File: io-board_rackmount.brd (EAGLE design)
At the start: 480.1 x 90.2 mm, 101 parts

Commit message: changed rackmounted IO board to single 8ch board
to be used with laser-cut mounting panel, or on its own
added pin headers for i2c and channels
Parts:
- removed CH10, CH11, CH12, CH13, CH14, CH15, CH16, CH17, CH18, CH19, CH20, CH21, CH22, CH23, CH24, CH25, CH26, CH27, CH28, CH29, CH30, CH31, CH32, CH9: BNC_VERTICAL, josh:BNC_VERTICAL
- removed LED10, LED11, LED12, LED13, LED14, LED15, LED16, LED17, LED18, LED19, LED20, LED21, LED22, LED23, LED24, LED25, LED26, LED27, LED28, LED29, LED30, LED31, LED32, LED9: (no value), sparkfun:LED3MM
- removed R10, R11, R12, R13, R14, R15, R16, R17, R18, R19, R20, R21, R22, R23, R24, R25, R26, R27, R28, R29, R30, R31, R32, R9: RESISTOR_PTH, josh:RESISTOR_PTH
- removed U$1, U$4, U$5: HDMI, open-ephys:HDMI_A
- added X1: 22-23-2041, con-molex:22-23-2041
- added X3: 22-23-2101, con-molex:22-23-2101
- moved U$2 75.3 mm to (-24.3, 84.3)
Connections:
- removed net CH1: CH10.P$1, R15.P$1, U$1.P$9
- removed net CH2: CH18.P$1, R23.P$1, U$4.P$9
- removed net CH3: CH26.P$1, R31.P$1, U$5.P$9
- removed net N$16: CH14.P$1, R11.P$2, U$1.P$3
- removed net N$17: CH13.P$1, R12.P$2, U$1.P$1
- removed net N$18: CH9.P$1, R16.P$1, U$1.P$7
- removed net N$19: CH11.P$1, R14.P$1, U$1.P$10
- removed net N$20: CH12.P$1, R13.P$1, U$1.P$12
- removed net N$21: CH16.P$1, R9.P$2, U$1.P$6
- removed net N$22: LED9.A, R13.P$2
- removed net N$24: LED10.A, R14.P$2
- removed net N$25: LED11.A, R15.P$2
- removed net N$26: LED12.A, R16.P$2
- removed net N$27: LED13.A, R9.P$1
- removed net N$28: LED14.A, R10.P$1
- removed net N$29: LED15.A, R11.P$1
- removed net N$30: LED16.A, R12.P$1
- removed net N$31: CH23.P$1, R18.P$2, U$4.P$4
- removed net N$32: CH22.P$1, R19.P$2, U$4.P$3
- removed net N$33: CH21.P$1, R20.P$2, U$4.P$1
- removed net N$34: CH17.P$1, R24.P$1, U$4.P$7
- removed net N$35: CH19.P$1, R22.P$1, U$4.P$10
- removed net N$36: CH20.P$1, R21.P$1, U$4.P$12
- removed net N$37: CH24.P$1, R17.P$2, U$4.P$6
- removed net N$38: LED17.A, R21.P$2
- removed net N$39: LED18.A, R22.P$2
- removed net N$40: LED19.A, R23.P$2
- removed net N$41: LED20.A, R24.P$2
- removed net N$42: LED21.A, R17.P$1
- removed net N$43: LED22.A, R18.P$1
- removed net N$44: LED23.A, R19.P$1
- removed net N$45: LED24.A, R20.P$1
- removed net N$46: CH31.P$1, R26.P$2, U$5.P$4
- removed net N$47: CH30.P$1, R27.P$2, U$5.P$3
- removed net N$48: CH29.P$1, R28.P$2, U$5.P$1
- removed net N$49: CH25.P$1, R32.P$1, U$5.P$7
- removed net N$50: CH27.P$1, R30.P$1, U$5.P$10
- removed net N$51: CH28.P$1, R29.P$1, U$5.P$12
- removed net N$52: CH32.P$1, R25.P$2, U$5.P$6
- removed net N$53: LED25.A, R29.P$2
- removed net N$54: LED26.A, R30.P$2
- removed net N$55: LED27.A, R31.P$2
- removed net N$56: LED28.A, R32.P$2
- removed net N$57: LED29.A, R25.P$1
- removed net N$58: LED30.A, R26.P$1
- removed net N$59: LED31.A, R27.P$1
- removed net N$6: CH15.P$1, R10.P$2, U$1.P$4
- removed net N$60: LED32.A, R28.P$1
- new net I2C_CLK: U$3.P$15, X1.3
- new net I2C_DAT: U$3.P$16, X1.4
- new net VCC: U$3.P$18, X1.2
- net CH6: now also X3.7
- net DGND: now also X1.1, X3.1, X3.10; no longer CH10.P$2, CH11.P$2, CH12.P$2, CH13.P$2, CH14.P$2, CH15.P$2, CH16.P$2, CH17.P$2, CH18.P$2, CH19.P$2, CH20.P$2, CH21.P$2, CH22.P$2, CH23.P$2, CH24.P$2, CH25.P$2, CH26.P$2, CH27.P$2, CH28.P$2, CH29.P$2, CH30.P$2, CH31.P$2, CH32.P$2, CH9.P$2, LED10.K, LED11.K, LED12.K, LED13.K, LED14.K, LED15.K, LED16.K, LED17.K, LED18.K, LED19.K, LED20.K, LED21.K, LED22.K, LED23.K, LED24.K, LED25.K, LED26.K, LED27.K, LED28.K, LED29.K, LED30.K, LED31.K, LED32.K, LED9.K, U$1.P$11, U$1.P$17, U$1.P$2, U$1.P$5, U$1.P$8, U$4.P$11, U$4.P$17, U$4.P$2, U$4.P$5, U$4.P$8, U$5.P$11, U$5.P$17, U$5.P$2, U$5.P$5, U$5.P$8
- net N$2: now also X3.4
- net N$23: now also X3.5
- net N$3: now also X3.3
- net N$4: now also X3.2
- net N$5: now also X3.6
- net N$7: now also X3.8
- net N$8: now also X3.9
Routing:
- net DGND: track 249.0 -> 72.4 mm, vias 14 -> 6
- net N$33: track 102.0 -> 0.00 mm, vias 2 -> 0
- net N$17: track 102.0 -> 0.00 mm, vias 2 -> 0
- net N$48: track 102.0 -> 0.00 mm, vias 2 -> 0
- net DGND2: track 100.6 -> 0.00 mm, vias 3 -> 0
- net N$16: track 100.0 -> 0.00 mm, vias 1 -> 0
- net N$32: track 100.0 -> 0.00 mm, vias 1 -> 0
- net N$47: track 100.0 -> 0.00 mm, vias 1 -> 0
- net N$52: track 82.3 -> 0.00 mm
- net N$37: track 82.3 -> 0.00 mm
- net N$21: track 82.3 -> 0.00 mm
- net N$18: track 81.3 -> 0.00 mm
- net N$49: track 81.3 -> 0.00 mm
- net N$34: track 81.3 -> 0.00 mm
- net S$14: track 0.00 -> 78.9 mm
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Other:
- board size 480.1 x 90.2 mm -> 122.7 x 90.3 mm
- board text added: "1 2 3 4 5 6 7 8"
- board text added: "5vdc"
- board text added: "gnd"
- board text added: "i2c clk"
- board text added: "i2c dat"

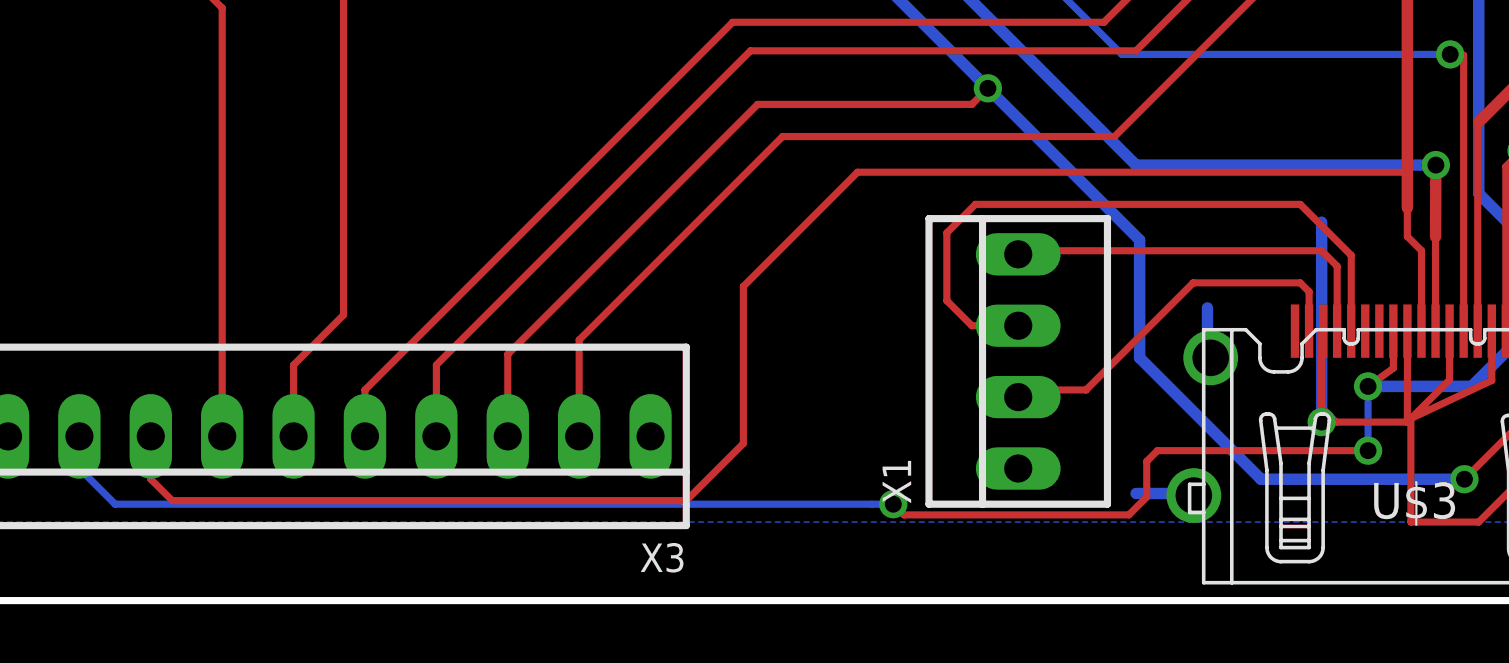
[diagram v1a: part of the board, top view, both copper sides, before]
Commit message: updated .1 inch connector to be linear
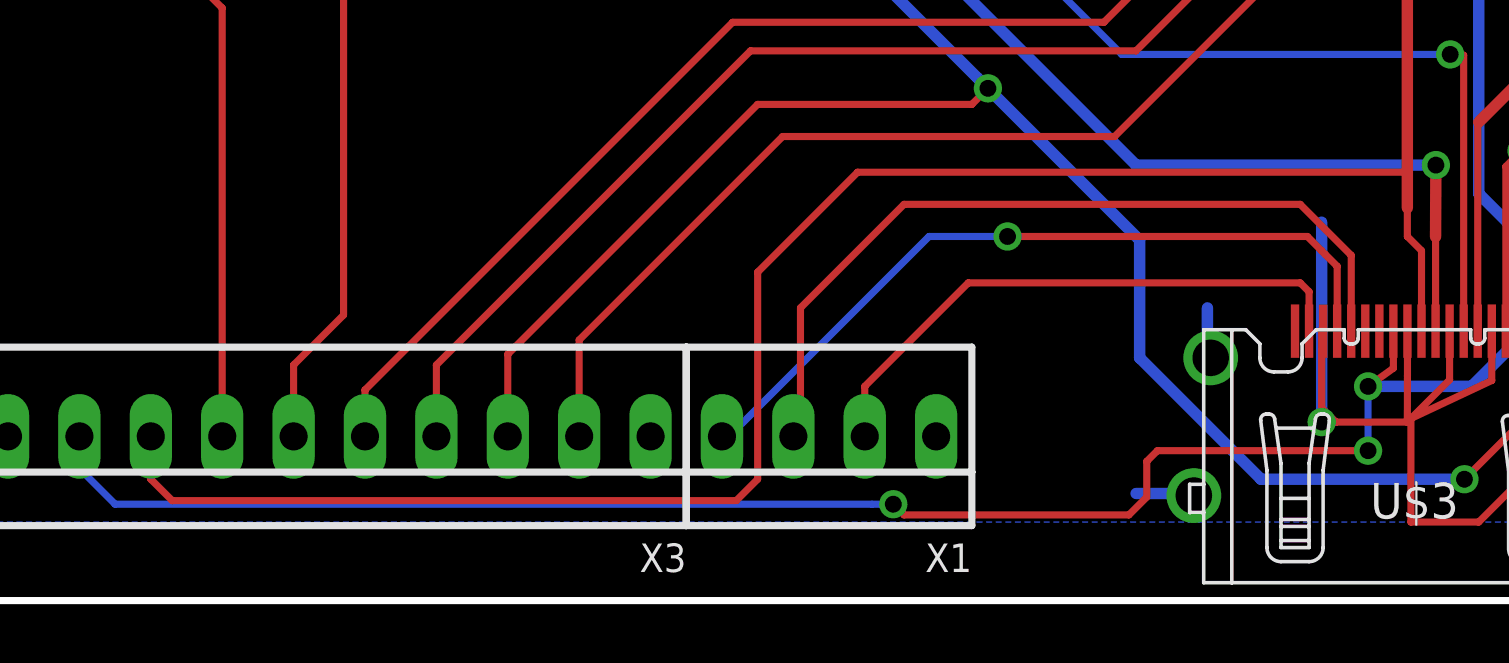
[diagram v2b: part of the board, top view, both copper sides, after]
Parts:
- moved X1 7.24 mm to (7.37, 4.57), turned to 180 degrees
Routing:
- net I2C_DAT: track 13.9 -> 27.6 mm, vias 0 -> 1
- net VCC: track 13.6 -> 20.9 mm
- net I2C_CLK: track 23.6 -> 29.2 mm
- net N$7: track 95.2 -> 96.3 mm
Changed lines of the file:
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@@
 <setting verticaltext="up"/>
 </settings>
-<grid distance="0.01" unitdist="inch" unit="inch" style="lines" multiple="10" display="yes" altdistance="0.025" altunitdist="inch" altunit="inch"/>
+<grid distance="10" unitdist="mil" unit="mil" style="lines" multiple="1" display="yes" altdistance="0.025" altunitdist="inch" altunit="inch"/>
 <layers>
 <layer number="1" name="Top" color="4" fill="1" visible="yes" active="yes"/>
@@
 <layer number="14" name="Route14" color="1" fill="6" visible="no" active="no"/>
 <layer number="15" name="Route15" color="4" fill="6" visible="no" active="no"/>
-<layer number="16" name="Bottom" color="9" fill="1" visible="no" active="yes"/>
+<layer number="16" name="Bottom" color="9" fill="1" visible="yes" active="yes"/>
 <layer number="17" name="Pads" color="2" fill="1" visible="yes" active="yes"/>
 <layer number="18" name="Vias" color="2" fill="1" visible="yes" active="yes"/>
@@
 <text x="68.072" y="45.72" size="6.096" layer="51" font="vector" ratio="16">8</text>
 <rectangle x1="39.624" y1="2.032" x2="73.152" y2="22.352" layer="51"/>
-<text x="6.858" y="2.794" size="1.27" layer="51" font="vector" ratio="12">gnd</text>
-<text x="5.842" y="5.207" size="1.27" layer="51" font="vector" ratio="12">5vdc</text>
-<text x="3.429" y="7.747" size="1.27" layer="51" font="vector" ratio="12">i2c clk</text>
-<text x="3.429" y="10.16" size="1.27" layer="51" font="vector" ratio="12">i2c dat</text>
+<text x="11.43" y="8.89" size="1.27" layer="51" font="vector" ratio="12" rot="R90">gnd</text>
+<text x="9.271" y="8.89" size="1.27" layer="51" font="vector" ratio="12" rot="R90">5vdc</text>
+<text x="6.731" y="8.509" size="1.27" layer="51" font="vector" ratio="12" rot="R90">i2c clk</text>
+<text x="4.318" y="8.255" size="1.27" layer="51" font="vector" ratio="12" rot="R90">i2c dat</text>
 <text x="-19.939" y="42.672" size="1.27" layer="25" font="vector" ratio="12">gnd</text>
 <text x="-21.209" y="8.255" size="1.27" layer="51" font="vector" ratio="12" rot="R90">gnd</text>
@@
 <element name="U$2" library="josh" package="OPEN_EPHYS_LOGO" value="" x="-24.257" y="84.328"/>
 <element name="U$3" library="open-ephys" package="HDMI_A" value="HDMI" x="28.194" y="7.366"/>
-<element name="X1" library="con-molex" package="22-23-2041" value="22-23-2041" x="14.097" y="7.239" rot="R90">
-<attribute name="OC_NEWARK" value="38C0355" x="14.097" y="7.239" size="1.778" layer="27" rot="R90" display="off"/>
-<attribute name="MPN" value="22-23-2041" x="14.097" y="7.239" size="1.778" layer="27" rot="R90" display="off"/>
-<attribute name="MF" value="MOLEX" x="14.097" y="7.239" size="1.778" layer="27" rot="R90" display="off"/>
-<attribute name="OC_FARNELL" value="1462920" x="14.097" y="7.239" size="1.778" layer="27" rot="R90" display="off"/>
+<element name="X1" library="con-molex" package="22-23-2041" value="22-23-2041" x="7.366" y="4.572" rot="R180">
+<attribute name="OC_NEWARK" value="38C0355" x="7.366" y="4.572" size="1.778" layer="27" rot="R180" display="off"/>
+<attribute name="MPN" value="22-23-2041" x="7.366" y="4.572" size="1.778" layer="27" rot="R180" display="off"/>
+<attribute name="MF" value="MOLEX" x="7.366" y="4.572" size="1.778" layer="27" rot="R180" display="off"/>
+<attribute name="OC_FARNELL" value="1462920" x="7.366" y="4.572" size="1.778" layer="27" rot="R180" display="off"/>
 </element>
 <element name="X3" library="con-molex" package="22-23-2101" value="22-23-2101" x="-10.414" y="4.572" rot="R180">
@@
 <wire x1="-16.764" y1="4.572" x2="-16.764" y2="3.048" width="0.254" layer="1"/>
 <wire x1="-16.764" y1="3.048" x2="-16.002" y2="2.286" width="0.254" layer="1"/>
-<wire x1="-16.002" y1="2.286" x2="2.286" y2="2.286" width="0.254" layer="1"/>
-<wire x1="2.286" y1="2.286" x2="4.318" y2="4.318" width="0.254" layer="1"/>
-<wire x1="4.318" y1="4.318" x2="4.318" y2="9.906" width="0.254" layer="1"/>
-<wire x1="4.318" y1="9.906" x2="8.382" y2="13.97" width="0.254" layer="1"/>
+<wire x1="-16.002" y1="2.286" x2="4.064" y2="2.286" width="0.254" layer="1"/>
+<wire x1="4.064" y1="2.286" x2="4.826" y2="3.048" width="0.254" layer="1"/>
+<wire x1="4.826" y1="3.048" x2="4.826" y2="10.414" width="0.254" layer="1"/>
+<wire x1="4.826" y1="10.414" x2="8.382" y2="13.97" width="0.254" layer="1"/>
 <wire x1="8.382" y1="13.97" x2="27.813" y2="13.97" width="0.254" layer="1"/>
 <wire x1="27.813" y1="13.97" x2="27.94" y2="14.097" width="0.254" layer="1"/>
@@
 <wire x1="24.444" y1="8.316" x2="24.444" y2="9.719" width="0.254" layer="1"/>
 <wire x1="24.444" y1="9.719" x2="24.13" y2="10.033" width="0.254" layer="1"/>
-<wire x1="24.13" y1="10.033" x2="20.32" y2="10.033" width="0.254" layer="1"/>
-<wire x1="20.32" y1="10.033" x2="16.51" y2="6.223" width="0.254" layer="1"/>
-<wire x1="16.51" y1="6.223" x2="14.351" y2="6.223" width="0.254" layer="1"/>
-<wire x1="14.351" y1="6.223" x2="14.097" y2="5.969" width="0.254" layer="1"/>
+<wire x1="24.13" y1="10.033" x2="12.319" y2="10.033" width="0.254" layer="1"/>
+<wire x1="12.319" y1="10.033" x2="8.636" y2="6.35" width="0.254" layer="1"/>
+<wire x1="8.636" y1="6.35" x2="8.636" y2="4.318" width="0.254" layer="1"/>
+<wire x1="8.636" y1="4.318" x2="8.636" y2="4.572" width="0" layer="19" extent="1-1"/>
 </signal>
 <signal name="I2C_CLK">
@@
 <wire x1="25.944" y1="8.316" x2="25.944" y2="11.013" width="0.254" layer="1"/>
 <wire x1="25.944" y1="11.013" x2="24.13" y2="12.827" width="0.254" layer="1"/>
-<wire x1="24.13" y1="12.827" x2="12.573" y2="12.827" width="0.254" layer="1"/>
-<wire x1="12.573" y1="12.827" x2="11.557" y2="11.811" width="0.254" layer="1"/>
-<wire x1="11.557" y1="11.811" x2="11.557" y2="9.398" width="0.254" layer="1"/>
-<wire x1="11.557" y1="9.398" x2="12.446" y2="8.509" width="0.254" layer="1"/>
-<wire x1="12.446" y1="8.509" x2="14.097" y2="8.509" width="0.254" layer="1"/>
+<wire x1="24.13" y1="12.827" x2="10.033" y2="12.827" width="0.254" layer="1"/>
+<wire x1="10.033" y1="12.827" x2="6.35" y2="9.144" width="0.254" layer="1"/>
+<wire x1="6.35" y1="9.144" x2="6.35" y2="4.826" width="0.254" layer="1"/>
+<wire x1="6.35" y1="4.826" x2="6.096" y2="4.572" width="0.254" layer="1"/>
 </signal>
 <signal name="I2C_DAT">
@@
 <contactref element="U$3" pad="P$16"/>
 <wire x1="25.444" y1="8.316" x2="25.444" y2="10.624" width="0.254" layer="1"/>
-<wire x1="25.444" y1="10.624" x2="24.892" y2="11.176" width="0.254" layer="1"/>
-<wire x1="24.892" y1="11.176" x2="14.224" y2="11.176" width="0.254" layer="1"/>
-<wire x1="14.224" y1="11.176" x2="14.097" y2="11.049" width="0.254" layer="1"/>
+<wire x1="25.444" y1="10.624" x2="25.019" y2="11.049" width="0.254" layer="1"/>
+<wire x1="25.019" y1="11.049" x2="24.892" y2="11.176" width="0.254" layer="1"/>
+<wire x1="3.556" y1="4.572" x2="3.81" y2="4.572" width="0.254" layer="16"/>
+<wire x1="3.81" y1="4.572" x2="10.922" y2="11.684" width="0.254" layer="16"/>
+<wire x1="10.922" y1="11.684" x2="13.716" y2="11.684" width="0.254" layer="16"/>
+<via x="13.716" y="11.684" extent="1-16" drill="0.6" shape="square"/>
+<wire x1="13.716" y1="11.684" x2="24.384" y2="11.684" width="0.254" layer="1"/>
+<wire x1="24.384" y1="11.684" x2="24.892" y2="11.176" width="0.254" layer="1"/>
 </signal>
 <signal name="DGND1">

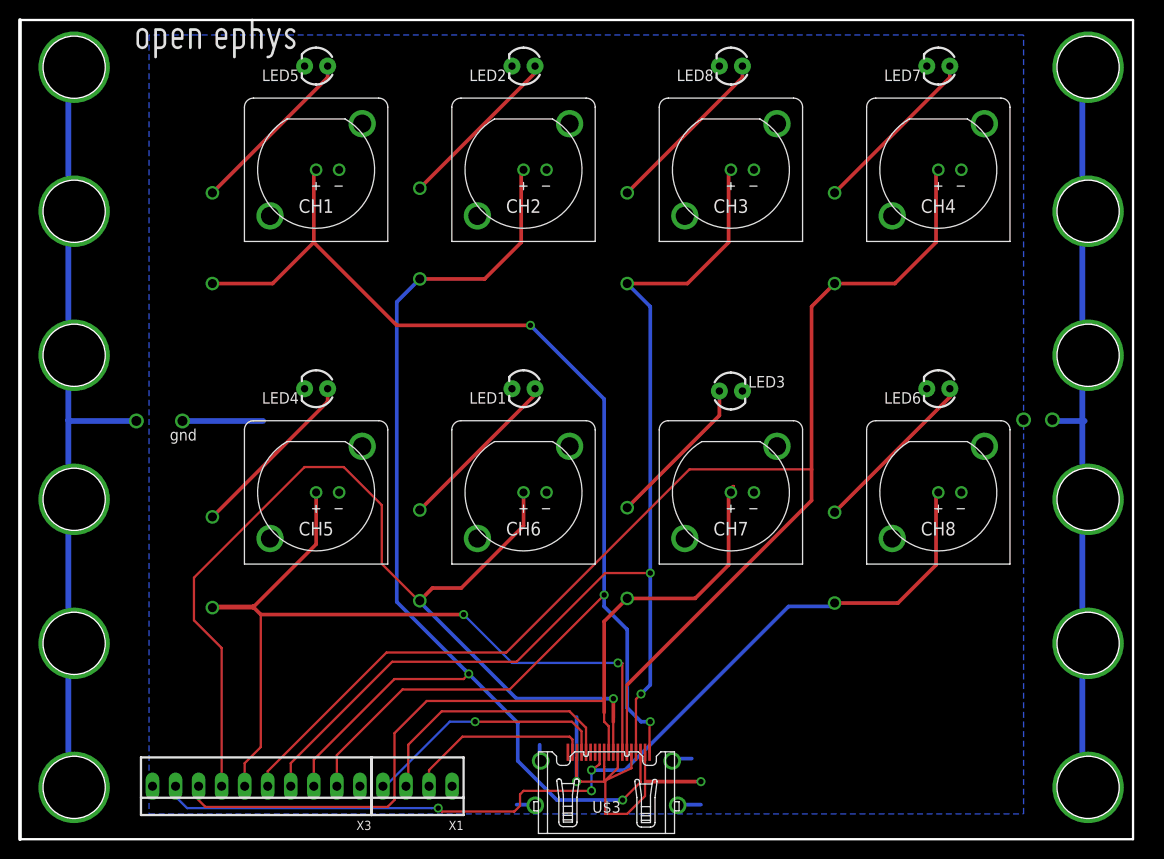
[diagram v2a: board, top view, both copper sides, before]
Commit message: Remove LEDs
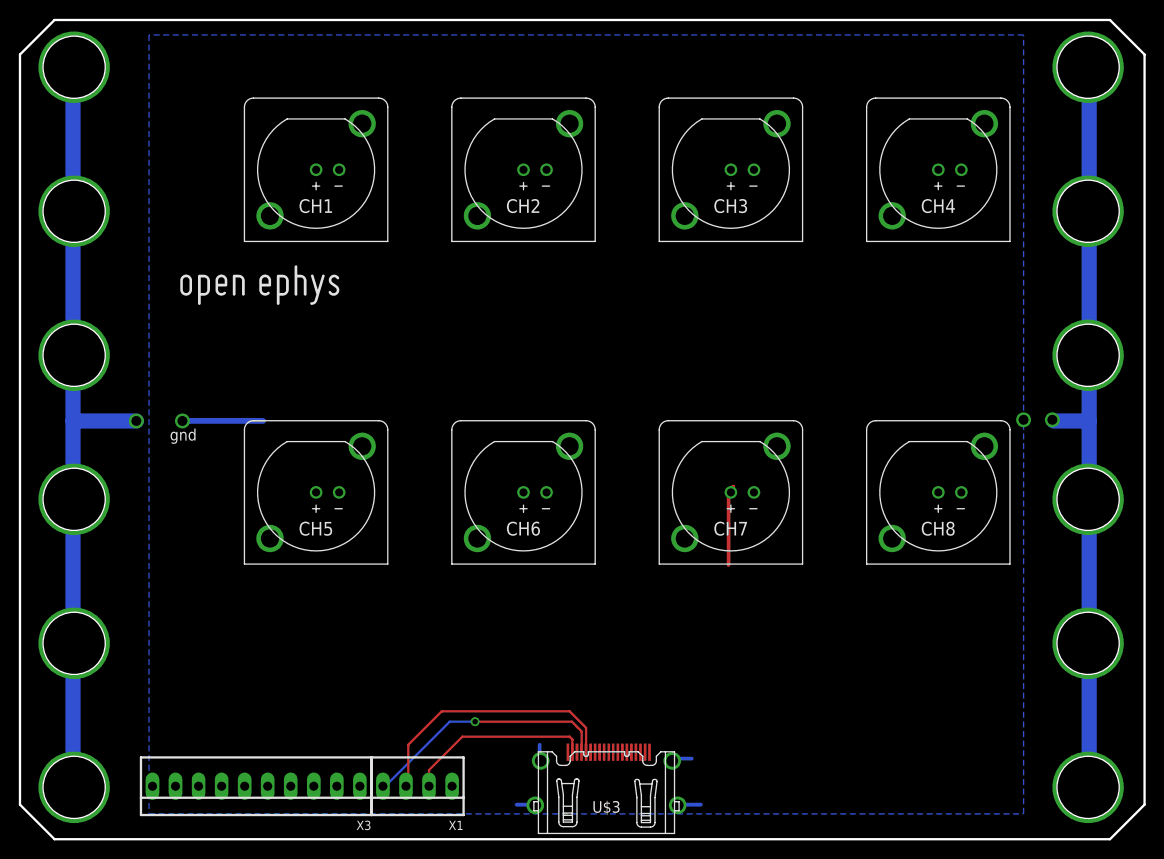
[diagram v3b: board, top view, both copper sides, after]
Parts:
- removed LED1, LED2, LED3, LED4, LED5, LED6, LED7, LED8: (no value), sparkfun:LED3MM
- removed R1, R2, R3, R4, R5, R6, R7, R8: RESISTOR_PTH, josh:RESISTOR_PTH
- moved U$2 27.6 mm to (-19.4, 57.1)
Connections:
- removed net N$1: LED6.A, R6.P$2
- removed net N$10: LED1.A, R1.P$2
- removed net N$11: LED4.A, R4.P$2
- removed net N$12: LED7.A, R7.P$1
- removed net N$13: LED8.A, R8.P$1
- removed net N$14: LED2.A, R2.P$1
- removed net N$15: LED5.A, R5.P$1
- removed net N$9: LED3.A, R3.P$2
- net CH6: no longer R1.P$1
- net DGND: no longer LED1.K, LED2.K, LED3.K, LED4.K, LED5.K, LED6.K, LED7.K, LED8.K
- net N$2: no longer R8.P$2
- net N$23: no longer R7.P$2
- net N$3: no longer R2.P$2
- net N$4: no longer R5.P$2
- net N$5: no longer R4.P$1
- net N$7: no longer R3.P$1
- net N$8: no longer R6.P$1
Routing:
- net N$23: track 157.7 -> 0.00 mm
- net N$4: track 142.2 -> 0.00 mm, vias 3 -> 0
- net N$2: track 125.4 -> 0.00 mm, vias 2 -> 0
- net N$3: track 124.0 -> 0.00 mm, vias 2 -> 0
- net CH6: track 115.4 -> 0.00 mm, vias 1 -> 0
- net N$8: track 109.5 -> 0.00 mm, vias 3 -> 0
- net N$5: track 97.5 -> 0.00 mm, vias 2 -> 0
- net N$7: track 96.3 -> 9.59 mm
- net DGND: track 72.4 -> 24.0 mm, vias 6 -> 4
- net N$11: track 19.4 -> 0.00 mm
- net N$15: track 19.2 -> 0.00 mm
- net N$13: track 19.2 -> 0.00 mm
- net N$12: track 19.2 -> 0.00 mm
- net N$1: track 18.9 -> 0.00 mm
- net N$14: track 18.7 -> 0.00 mm
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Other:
- board size 122.7 x 90.3 mm -> 124 x 90.3 mm
- board text added: "May 2013"
- board text added: "version 1.3"
- board text removed: "mar 2013"
- board text removed: "version 1.2"

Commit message: Redo rounting
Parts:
- moved X1 36.7 mm to (43.9, 7.37)
- moved X3 36.7 mm to (26.2, 7.37), turned to 0 degrees
- moved U$3 36.6 mm to (64.8, 9.40)
- moved CH3 36.6 mm to (78.5, 74.3)
- moved CH4 36.6 mm to (101.3, 74.3)
- moved CH7 36.6 mm to (78.5, 38.7)
- moved CH8 36.6 mm to (101.3, 38.7)
- moved CH1 36.6 mm to (32.8, 74.3)
- moved CH5 36.6 mm to (32.8, 38.7)
- moved U$2 36.6 mm to (17.1, 58.9)
- moved CH2 36.6 mm to (55.6, 74.3)
- moved CH6 36.6 mm to (55.6, 38.7)
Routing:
- net N$23: track 0.00 -> 182.4 mm
- net N$2: track 0.00 -> 165.2 mm
- net N$3: track 0.00 -> 153.1 mm
- net N$4: track 0.00 -> 137.9 mm
- net N$8: track 0.00 -> 137.1 mm
- net N$7: track 9.59 -> 120.9 mm
- net CH6: track 0.00 -> 104.7 mm
- net N$5: track 0.00 -> 91.6 mm
- net DGND: track 24.0 -> 54.8 mm, vias 4 -> 9
- net VCC: track 20.9 -> 19.6 mm
- net I2C_CLK: track 29.2 -> 28.0 mm
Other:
- board text added: "8 7 6 5 4 3 2 1"
- board text removed: "1 2 3 4 5 6 7 8"
